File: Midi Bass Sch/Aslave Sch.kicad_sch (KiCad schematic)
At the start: 12 parts, among them J4 A SLAVE ISCP, SW4 A-slave Reset, U6 PIC16F1789

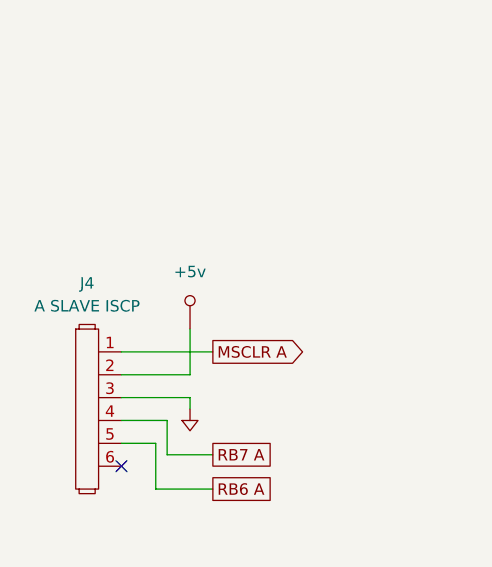
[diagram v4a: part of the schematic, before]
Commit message: started basic pcb layout for Master pic
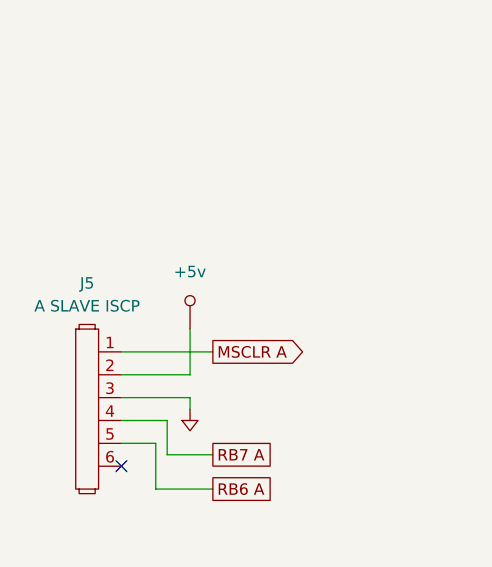
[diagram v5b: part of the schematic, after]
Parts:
- renumbered J4 to J5
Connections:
- net MSCLR A: now also D14.1; no longer D14.2
- net at C4.1, R47.1, SW4.2: now also D14.2; no longer D14.1
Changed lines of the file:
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@@
 		(dnp no)
 		(fields_autoplaced yes)
-		(property "Reference" "#PWR061"
+		(property "Reference" "#PWR063"
 			(at 36.83 135.89 0)
 			(effects
@@
 			(project "Midi Bass Sch"
 				(path "/06818073-fb22-48ee-acc5-6dedd827034e/c3b9cd48-3fcf-4fda-9d60-ef0911073906"
-					(reference "#PWR061")
+					(reference "#PWR063")
 					(unit 1)
 				)
@@
 		(dnp no)
 		(fields_autoplaced yes)
-		(property "Reference" "#PWR064"
+		(property "Reference" "#PWR066"
 			(at 63.1444 113.1316 0)
 			(effects
@@
 			(project "Midi Bass Sch"
 				(path "/06818073-fb22-48ee-acc5-6dedd827034e/c3b9cd48-3fcf-4fda-9d60-ef0911073906"
-					(reference "#PWR064")
+					(reference "#PWR066")
 					(unit 1)
 				)
@@
 		(dnp no)
 		(fields_autoplaced yes)
-		(property "Reference" "#PWR069"
+		(property "Reference" "#PWR071"
 			(at 200.66 119.38 0)
 			(effects
@@
 			(project "Midi Bass Sch"
 				(path "/06818073-fb22-48ee-acc5-6dedd827034e/c3b9cd48-3fcf-4fda-9d60-ef0911073906"
-					(reference "#PWR069")
+					(reference "#PWR071")
 					(unit 1)
 				)
@@
 		(dnp no)
 		(fields_autoplaced yes)
-		(property "Reference" "#PWR066"
+		(property "Reference" "#PWR068"
 			(at 113.03 153.67 0)
 			(effects
@@
 			(project "Midi Bass Sch"
 				(path "/06818073-fb22-48ee-acc5-6dedd827034e/c3b9cd48-3fcf-4fda-9d60-ef0911073906"
-					(reference "#PWR066")
+					(reference "#PWR068")
 					(unit 1)
 				)
@@
 		(dnp no)
 		(fields_autoplaced yes)
-		(property "Reference" "#PWR062"
+		(property "Reference" "#PWR064"
 			(at 46.6344 50.9016 0)
 			(effects
@@
 			(project "Midi Bass Sch"
 				(path "/06818073-fb22-48ee-acc5-6dedd827034e/c3b9cd48-3fcf-4fda-9d60-ef0911073906"
-					(reference "#PWR062")
+					(reference "#PWR064")
 					(unit 1)
 				)
@@
 		(dnp no)
 		(fields_autoplaced yes)
-		(property "Reference" "#PWR063"
+		(property "Reference" "#PWR065"
 			(at 41.91 63.5 0)
 			(effects
@@
 			(project "Midi Bass Sch"
 				(path "/06818073-fb22-48ee-acc5-6dedd827034e/c3b9cd48-3fcf-4fda-9d60-ef0911073906"
-					(reference "#PWR063")
+					(reference "#PWR065")
 					(unit 1)
 				)
@@
 		(dnp no)
 		(fields_autoplaced yes)
-		(property "Reference" "#PWR067"
+		(property "Reference" "#PWR069"
 			(at 120.2944 16.6116 0)
 			(effects
@@
 			(project "Midi Bass Sch"
 				(path "/06818073-fb22-48ee-acc5-6dedd827034e/c3b9cd48-3fcf-4fda-9d60-ef0911073906"
-					(reference "#PWR067")
+					(reference "#PWR069")
 					(unit 1)
 				)
@@
 		(dnp no)
 		(fields_autoplaced yes)
-		(property "Reference" "#PWR065"
+		(property "Reference" "#PWR067"
 			(at 58.42 134.62 0)
 			(effects
@@
 			(project "Midi Bass Sch"
 				(path "/06818073-fb22-48ee-acc5-6dedd827034e/c3b9cd48-3fcf-4fda-9d60-ef0911073906"
-					(reference "#PWR065")
+					(reference "#PWR067")
 					(unit 1)
 				)
@@
 		(dnp no)
 		(fields_autoplaced yes)
-		(property "Reference" "J4"
+		(property "Reference" "J5"
 			(at 30.48 50.8 0)
 			(effects
@@
 			(project "Midi Bass Sch"
 				(path "/06818073-fb22-48ee-acc5-6dedd827034e/c3b9cd48-3fcf-4fda-9d60-ef0911073906"
-					(reference "J4")
+					(reference "J5")
 					(unit 1)
 				)
@@
 		(dnp no)
 		(fields_autoplaced yes)
-		(property "Reference" "#PWR068"
+		(property "Reference" "#PWR070"
 			(at 186.69 121.92 0)
 			(effects
@@
 			(project "Midi Bass Sch"
 				(path "/06818073-fb22-48ee-acc5-6dedd827034e/c3b9cd48-3fcf-4fda-9d60-ef0911073906"
-					(reference "#PWR068")
-					(unit 1)
-				)
+					(reference "#PWR070")
+					(unit 1)
+				)

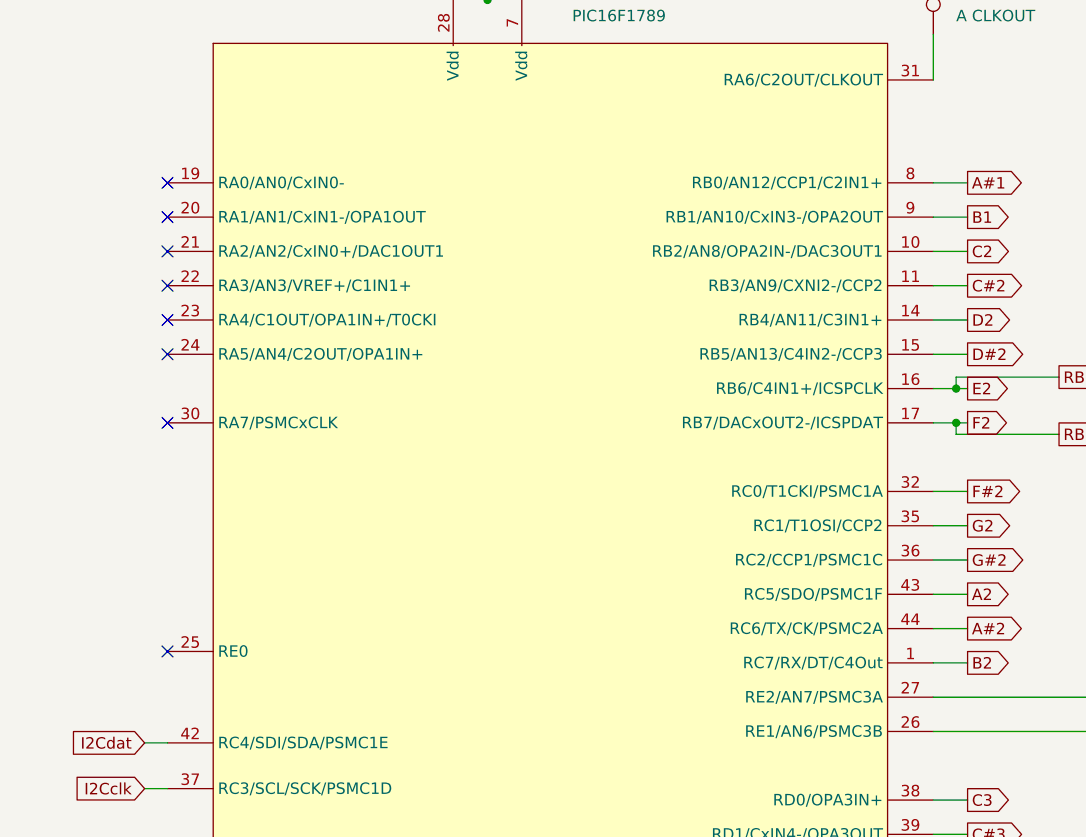
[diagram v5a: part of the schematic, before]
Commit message: updated schematic to reflect code
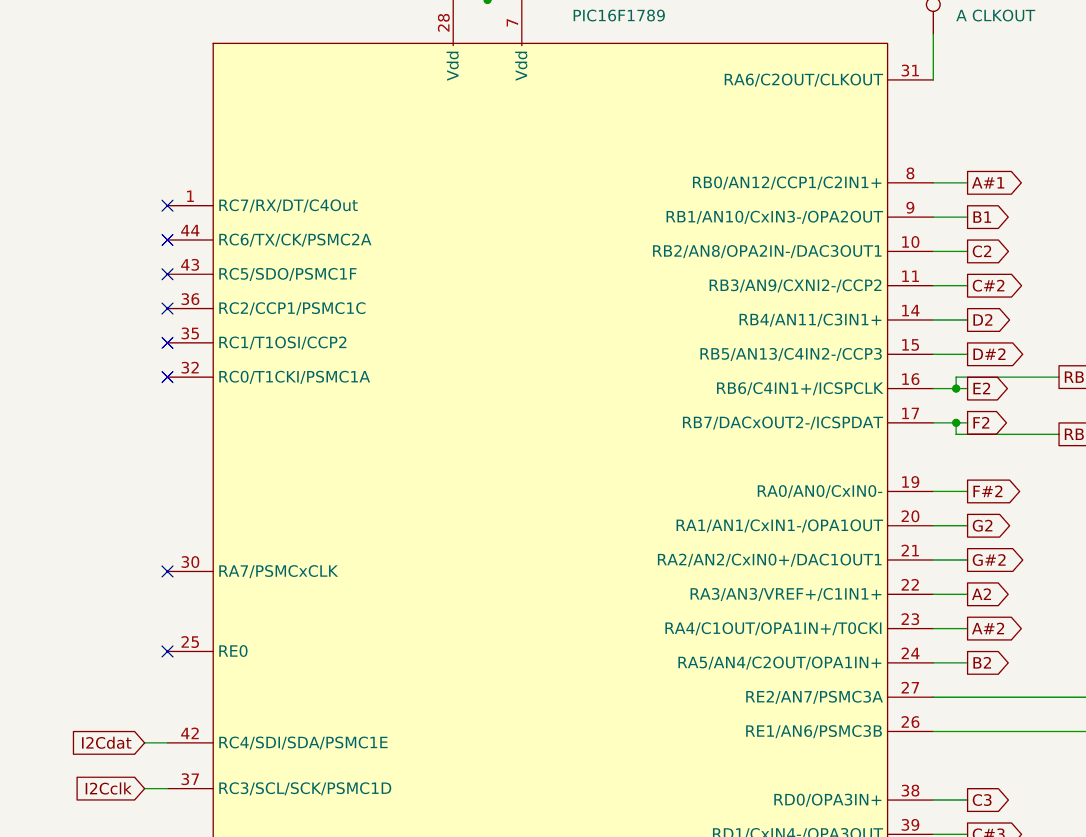
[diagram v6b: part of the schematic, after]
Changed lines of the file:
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@@
 	)
 	(no_connect
-		(at 80.01 69.85)
+		(at 80.01 86.36)
 	)
 	(no_connect
-		(at 80.01 46.99)
+		(at 80.01 49.53)
 	)
 	(no_connect
-		(at 80.01 58.42)
+		(at 80.01 60.96)
 	)
 	(no_connect
-		(at 80.01 43.18)
+		(at 80.01 45.72)
 	)
 	(no_connect
@@
 	)
 	(no_connect
-		(at 80.01 62.23)
+		(at 80.01 64.77)
 	)
 	(no_connect
@@
 	)
 	(no_connect
-		(at 80.01 50.8)
+		(at 80.01 53.34)
 	)
 	(no_connect
@@
 	)
 	(no_connect
-		(at 80.01 54.61)
+		(at 80.01 57.15)
 	)
 	(wire

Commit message: working on troubleshooting section of report
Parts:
- renumbered J5 to J6, R46 to R58, R47 to R59, R48 to R60, R49 to R61, U6 to U8
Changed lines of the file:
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@@
 		(dnp no)
 		(fields_autoplaced yes)
-		(property "Reference" "#PWR063"
+		(property "Reference" "#PWR077"
 			(at 36.83 135.89 0)
 			(effects
@@
 			(project "Midi Bass Sch"
 				(path "/06818073-fb22-48ee-acc5-6dedd827034e/c3b9cd48-3fcf-4fda-9d60-ef0911073906"
-					(reference "#PWR063")
+					(reference "#PWR077")
 					(unit 1)
 				)
@@
 		(dnp no)
 		(fields_autoplaced yes)
-		(property "Reference" "#PWR066"
+		(property "Reference" "#PWR080"
 			(at 63.1444 113.1316 0)
 			(effects
@@
 			(project "Midi Bass Sch"
 				(path "/06818073-fb22-48ee-acc5-6dedd827034e/c3b9cd48-3fcf-4fda-9d60-ef0911073906"
-					(reference "#PWR066")
+					(reference "#PWR080")
 					(unit 1)
 				)
@@
 		(dnp no)
 		(fields_autoplaced yes)
-		(property "Reference" "#PWR071"
+		(property "Reference" "#PWR085"
 			(at 200.66 119.38 0)
 			(effects
@@
 			(project "Midi Bass Sch"
 				(path "/06818073-fb22-48ee-acc5-6dedd827034e/c3b9cd48-3fcf-4fda-9d60-ef0911073906"
-					(reference "#PWR071")
+					(reference "#PWR085")
 					(unit 1)
 				)
@@
 		(dnp no)
 		(fields_autoplaced yes)
-		(property "Reference" "R48"
+		(property "Reference" "R60"
 			(at 189.23 107.9499 90)
 			(effects
@@
 			(project "Midi Bass Sch"
 				(path "/06818073-fb22-48ee-acc5-6dedd827034e/c3b9cd48-3fcf-4fda-9d60-ef0911073906"
-					(reference "R48")
+					(reference "R60")
 					(unit 1)
 				)
@@
 		(dnp no)
 		(fields_autoplaced yes)
-		(property "Reference" "R46"
+		(property "Reference" "R58"
 			(at 39.37 132.0799 90)
 			(effects
@@
 			(project "Midi Bass Sch"
 				(path "/06818073-fb22-48ee-acc5-6dedd827034e/c3b9cd48-3fcf-4fda-9d60-ef0911073906"
-					(reference "R46")
+					(reference "R58")
 					(unit 1)
 				)
@@
 		(dnp no)
 		(fields_autoplaced yes)
-		(property "Reference" "#PWR068"
+		(property "Reference" "#PWR082"
 			(at 113.03 153.67 0)
 			(effects
@@
 			(project "Midi Bass Sch"
 				(path "/06818073-fb22-48ee-acc5-6dedd827034e/c3b9cd48-3fcf-4fda-9d60-ef0911073906"
-					(reference "#PWR068")
+					(reference "#PWR082")
 					(unit 1)
 				)
@@
 		(dnp no)
 		(fields_autoplaced yes)
-		(property "Reference" "R47"
+		(property "Reference" "R59"
 			(at 60.96 120.6499 90)
 			(effects
@@
 			(project "Midi Bass Sch"
 				(path "/06818073-fb22-48ee-acc5-6dedd827034e/c3b9cd48-3fcf-4fda-9d60-ef0911073906"
-					(reference "R47")
+					(reference "R59")
 					(unit 1)
 				)
@@
 		(dnp no)
 		(fields_autoplaced yes)
-		(property "Reference" "#PWR064"
+		(property "Reference" "#PWR078"
 			(at 46.6344 50.9016 0)
 			(effects
@@
 			(project "Midi Bass Sch"
 				(path "/06818073-fb22-48ee-acc5-6dedd827034e/c3b9cd48-3fcf-4fda-9d60-ef0911073906"
-					(reference "#PWR064")
+					(reference "#PWR078")
 					(unit 1)
 				)
@@
 		(dnp no)
 		(fields_autoplaced yes)
-		(property "Reference" "#PWR065"
+		(property "Reference" "#PWR079"
 			(at 41.91 63.5 0)
 			(effects
@@
 			(project "Midi Bass Sch"
 				(path "/06818073-fb22-48ee-acc5-6dedd827034e/c3b9cd48-3fcf-4fda-9d60-ef0911073906"
-					(reference "#PWR065")
+					(reference "#PWR079")
 					(unit 1)
 				)
@@
 		(dnp no)
 		(fields_autoplaced yes)
-		(property "Reference" "#PWR069"
+		(property "Reference" "#PWR083"
 			(at 120.2944 16.6116 0)
 			(effects
@@
 			(project "Midi Bass Sch"
 				(path "/06818073-fb22-48ee-acc5-6dedd827034e/c3b9cd48-3fcf-4fda-9d60-ef0911073906"
-					(reference "#PWR069")
+					(reference "#PWR083")
 					(unit 1)
 				)
@@
 		(on_board yes)
 		(dnp no)
-		(property "Reference" "U6"
+		(property "Reference" "U8"
 			(at 124.968 21.59 0)
 			(effects
@@
 			(project "Midi Bass Sch"
 				(path "/06818073-fb22-48ee-acc5-6dedd827034e/c3b9cd48-3fcf-4fda-9d60-ef0911073906"
-					(reference "U6")
+					(reference "U8")
 					(unit 1)
 				)
@@
 		(dnp no)
 		(fields_autoplaced yes)
-		(property "Reference" "R49"
+		(property "Reference" "R61"
 			(at 203.2 105.4099 90)
 			(effects
@@
 			(project "Midi Bass Sch"
 				(path "/06818073-fb22-48ee-acc5-6dedd827034e/c3b9cd48-3fcf-4fda-9d60-ef0911073906"
-					(reference "R49")
+					(reference "R61")
 					(unit 1)
 				)
@@
 		(dnp no)
 		(fields_autoplaced yes)
-		(property "Reference" "#PWR067"
+		(property "Reference" "#PWR081"
 			(at 58.42 134.62 0)
 			(effects
@@
 			(project "Midi Bass Sch"
 				(path "/06818073-fb22-48ee-acc5-6dedd827034e/c3b9cd48-3fcf-4fda-9d60-ef0911073906"
-					(reference "#PWR067")
+					(reference "#PWR081")
 					(unit 1)
 				)
@@
 		(dnp no)
 		(fields_autoplaced yes)
-		(property "Reference" "J5"
+		(property "Reference" "J6"
 			(at 30.48 50.8 0)
 			(effects
@@
 			(project "Midi Bass Sch"
 				(path "/06818073-fb22-48ee-acc5-6dedd827034e/c3b9cd48-3fcf-4fda-9d60-ef0911073906"
-					(reference "J5")
+					(reference "J6")
 					(unit 1)
 				)
@@
 		(dnp no)
 		(fields_autoplaced yes)
-		(property "Reference" "#PWR070"
+		(property "Reference" "#PWR084"
 			(at 186.69 121.92 0)
 			(effects
@@
 			(project "Midi Bass Sch"
 				(path "/06818073-fb22-48ee-acc5-6dedd827034e/c3b9cd48-3fcf-4fda-9d60-ef0911073906"
-					(reference "#PWR070")
-					(unit 1)
-				)
+					(reference "#PWR084")
+					(unit 1)
+				)

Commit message: working on final troubleshooting sections, modified pluck slave to header connections
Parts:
- renumbered J6 to J8
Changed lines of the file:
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@@
 		(dnp no)
 		(fields_autoplaced yes)
-		(property "Reference" "#PWR077"
+		(property "Reference" "#PWR079"
 			(at 36.83 135.89 0)
 			(effects
@@
 			(project "Midi Bass Sch"
 				(path "/06818073-fb22-48ee-acc5-6dedd827034e/c3b9cd48-3fcf-4fda-9d60-ef0911073906"
-					(reference "#PWR077")
+					(reference "#PWR079")
 					(unit 1)
 				)
@@
 		(dnp no)
 		(fields_autoplaced yes)
-		(property "Reference" "#PWR080"
+		(property "Reference" "#PWR082"
 			(at 63.1444 113.1316 0)
 			(effects
@@
 			(project "Midi Bass Sch"
 				(path "/06818073-fb22-48ee-acc5-6dedd827034e/c3b9cd48-3fcf-4fda-9d60-ef0911073906"
-					(reference "#PWR080")
+					(reference "#PWR082")
 					(unit 1)
 				)
@@
 		(dnp no)
 		(fields_autoplaced yes)
-		(property "Reference" "#PWR085"
+		(property "Reference" "#PWR087"
 			(at 200.66 119.38 0)
 			(effects
@@
 			(project "Midi Bass Sch"
 				(path "/06818073-fb22-48ee-acc5-6dedd827034e/c3b9cd48-3fcf-4fda-9d60-ef0911073906"
-					(reference "#PWR085")
+					(reference "#PWR087")
 					(unit 1)
 				)
@@
 		(dnp no)
 		(fields_autoplaced yes)
-		(property "Reference" "#PWR082"
+		(property "Reference" "#PWR084"
 			(at 113.03 153.67 0)
 			(effects
@@
 			(project "Midi Bass Sch"
 				(path "/06818073-fb22-48ee-acc5-6dedd827034e/c3b9cd48-3fcf-4fda-9d60-ef0911073906"
-					(reference "#PWR082")
+					(reference "#PWR084")
 					(unit 1)
 				)
@@
 		(dnp no)
 		(fields_autoplaced yes)
-		(property "Reference" "#PWR078"
+		(property "Reference" "#PWR080"
 			(at 46.6344 50.9016 0)
 			(effects
@@
 			(project "Midi Bass Sch"
 				(path "/06818073-fb22-48ee-acc5-6dedd827034e/c3b9cd48-3fcf-4fda-9d60-ef0911073906"
-					(reference "#PWR078")
+					(reference "#PWR080")
 					(unit 1)
 				)
@@
 		(dnp no)
 		(fields_autoplaced yes)
-		(property "Reference" "#PWR079"
+		(property "Reference" "#PWR081"
 			(at 41.91 63.5 0)
 			(effects
@@
 			(project "Midi Bass Sch"
 				(path "/06818073-fb22-48ee-acc5-6dedd827034e/c3b9cd48-3fcf-4fda-9d60-ef0911073906"
-					(reference "#PWR079")
+					(reference "#PWR081")
 					(unit 1)
 				)
@@
 		(dnp no)
 		(fields_autoplaced yes)
-		(property "Reference" "#PWR083"
+		(property "Reference" "#PWR085"
 			(at 120.2944 16.6116 0)
 			(effects
@@
 			(project "Midi Bass Sch"
 				(path "/06818073-fb22-48ee-acc5-6dedd827034e/c3b9cd48-3fcf-4fda-9d60-ef0911073906"
-					(reference "#PWR083")
+					(reference "#PWR085")
 					(unit 1)
 				)
@@
 		(dnp no)
 		(fields_autoplaced yes)
-		(property "Reference" "#PWR081"
+		(property "Reference" "#PWR083"
 			(at 58.42 134.62 0)
 			(effects
@@
 			(project "Midi Bass Sch"
 				(path "/06818073-fb22-48ee-acc5-6dedd827034e/c3b9cd48-3fcf-4fda-9d60-ef0911073906"
-					(reference "#PWR081")
+					(reference "#PWR083")
 					(unit 1)
 				)
@@
 		(dnp no)
 		(fields_autoplaced yes)
-		(property "Reference" "J6"
+		(property "Reference" "J8"
 			(at 30.48 50.8 0)
 			(effects
@@
 			(project "Midi Bass Sch"
 				(path "/06818073-fb22-48ee-acc5-6dedd827034e/c3b9cd48-3fcf-4fda-9d60-ef0911073906"
-					(reference "J6")
+					(reference "J8")
 					(unit 1)
 				)
@@
 		(dnp no)
 		(fields_autoplaced yes)
-		(property "Reference" "#PWR084"
+		(property "Reference" "#PWR086"
 			(at 186.69 121.92 0)
 			(effects
@@
 			(project "Midi Bass Sch"
 				(path "/06818073-fb22-48ee-acc5-6dedd827034e/c3b9cd48-3fcf-4fda-9d60-ef0911073906"
-					(reference "#PWR084")
-					(unit 1)
-				)
+					(reference "#PWR086")
+					(unit 1)
+				)
